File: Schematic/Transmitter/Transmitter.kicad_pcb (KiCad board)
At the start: 2 copper layers, 141.8 x 96.5 mm, 4 parts, among them J2 Remote Umbilical, U1 Mini360, U2 RFM69HW, U3 BP

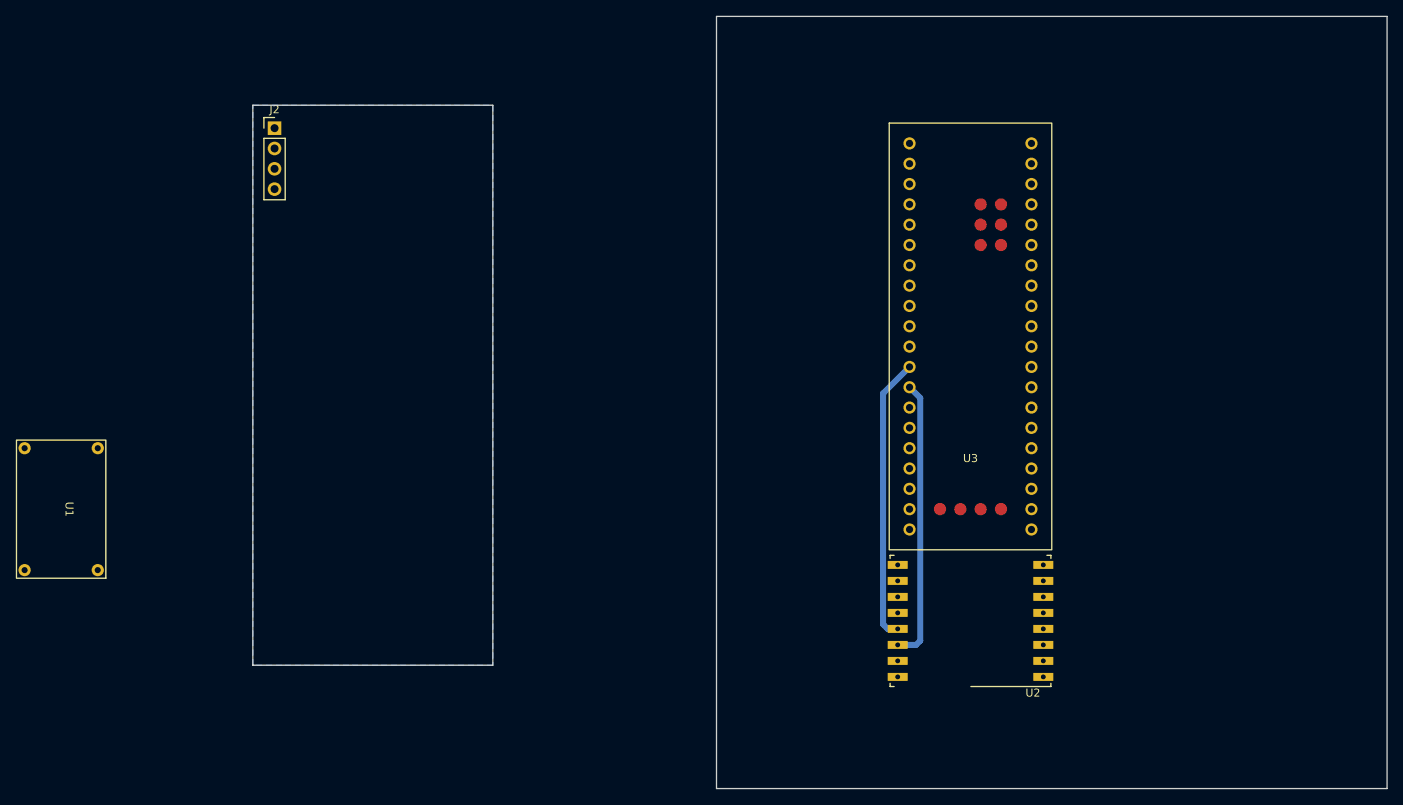
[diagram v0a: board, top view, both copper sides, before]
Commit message: Add transmitter PCB
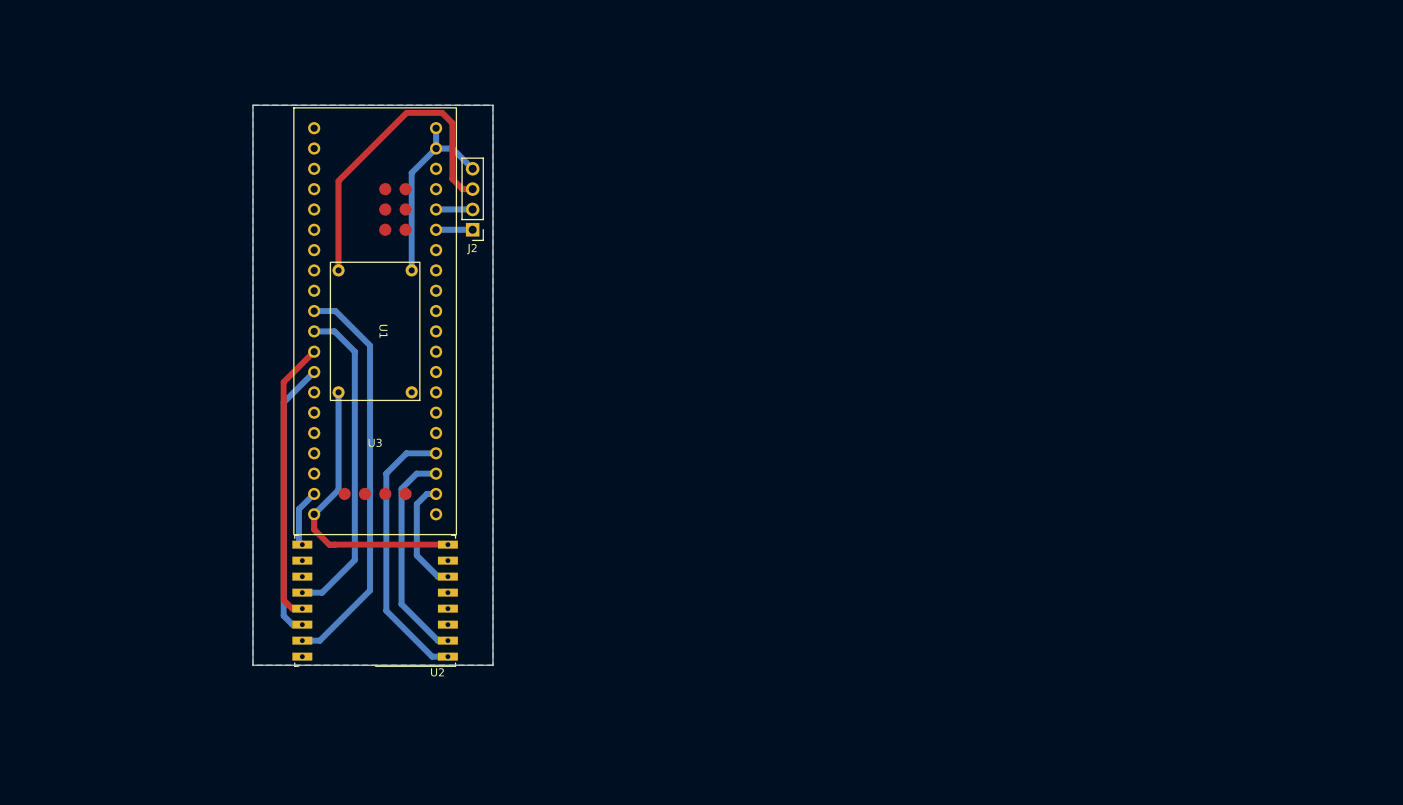
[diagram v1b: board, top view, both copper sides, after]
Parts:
- moved U2 74.5 mm to (145.3, 121.9)
- moved U3 74.4 mm to (145.3, 85.7)
- moved U1 45.1 mm to (145.3, 88.3)
- moved J2 27.8 mm to (157.5, 75.6), turned to 180 degrees
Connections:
- U3 pad PA0: /PPM IN -> unconnected-(U3-PadPA0)
- U3 pad PA1: /PPM OUT -> unconnected-(U3-PadPA1)
- U3 pad PA4: /NSS -> unconnected-(U3-PadPA4)
- U3 pad PA5: /SCK -> unconnected-(U3-PadPA5)
- U3 pad PA6: /MISO -> unconnected-(U3-PadPA6)
- U3 pad PA7: /MOSI -> unconnected-(U3-PadPA7)
- U3 pad PB10: unconnected-(U3-PadPB10) -> /PPM OUT
- U3 pad PB11: unconnected-(U3-PadPB11) -> /PPM IN
- U3 pad PB12: /NSS -> unconnected-(U3-PadPB12)
- U3 pad PB13: /SCK -> unconnected-(U3-PadPB13)
- U3 pad PB14: /MISO -> unconnected-(U3-PadPB14)
- U3 pad PB15: /MOSI -> unconnected-(U3-PadPB15)
- U3 pad PB6: /AUX -> unconnected-(U3-PadPB6)
- U3 pad PB7: /INTER -> unconnected-(U3-PadPB7)
- U3 pad PB8: /RESET -> unconnected-(U3-PadPB8)
- U3 pad PC13: unconnected-(U3-PadPC13) -> /AUX
- U3 pad PC14: unconnected-(U3-PadPC14) -> /INTER
- U3 pad PC15: unconnected-(U3-PadPC15) -> /RESET
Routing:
- net /NSS: track 0.00 -> 50.4 mm
- net /SCK: track 0.00 -> 40.4 mm
- net +BATT: track 0.00 -> 39.5 mm
- net +3V3: track 0.00 -> 35.9 mm
- net /RESET: track 0.00 -> 34.5 mm
- net GND: track 0.00 -> 32.0 mm
- net /INTER: track 0.00 -> 27.2 mm
- net /AUX: track 0.00 -> 14.4 mm
- net /PPM IN: track 0.00 -> 4.57 mm
- net /PPM OUT: track 0.00 -> 4.57 mm
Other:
- board size 141.8 x 96.5 mm -> 30 x 70 mm

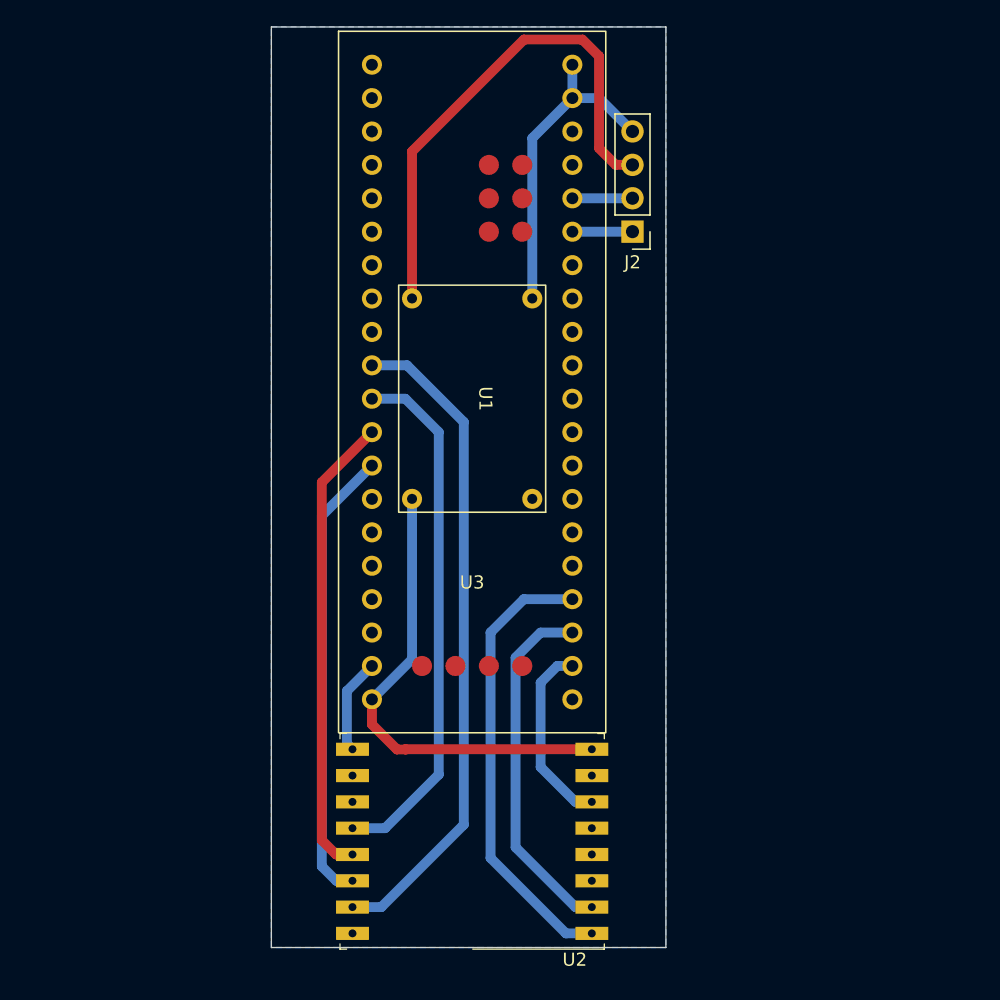
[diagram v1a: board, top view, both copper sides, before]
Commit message: combine schematics into a single PCB layout
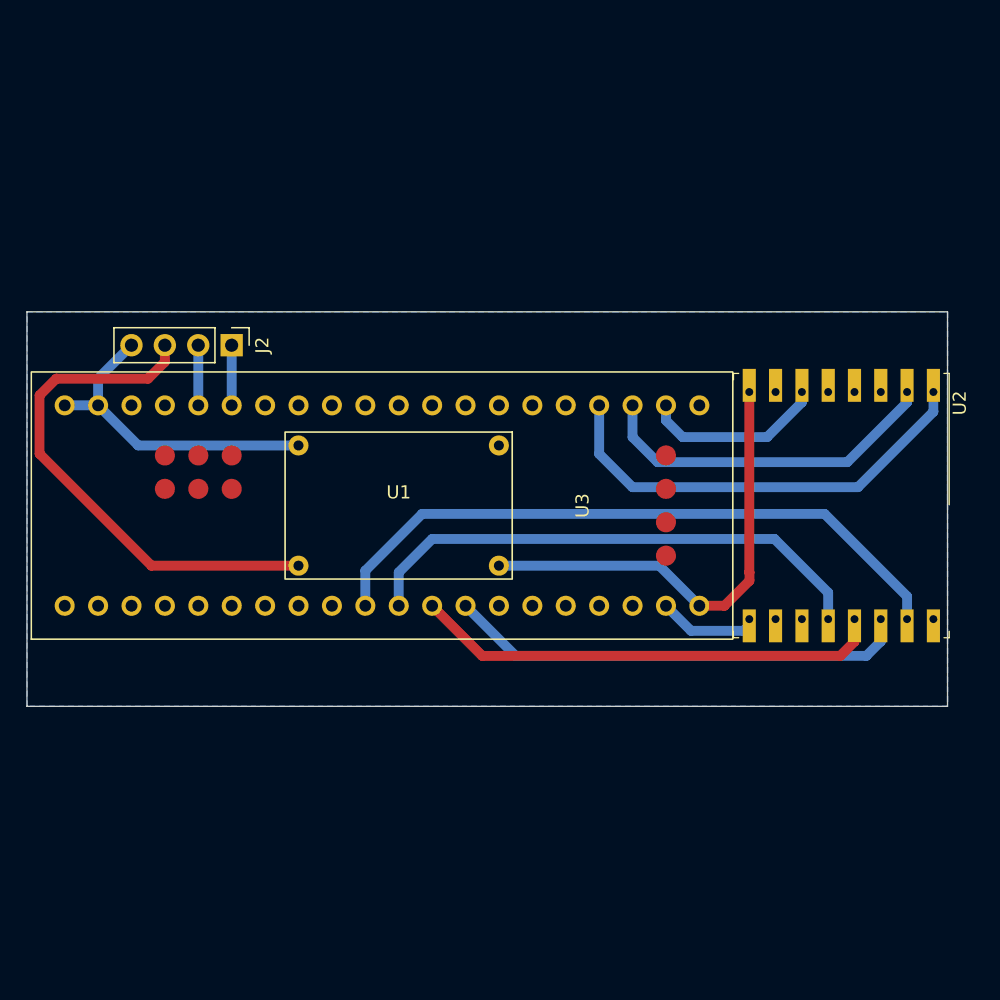
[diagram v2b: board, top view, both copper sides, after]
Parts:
- moved U2 37.9 mm to (173.4, 96.4), turned to -90 degrees
- moved J2 31.7 mm to (127.0, 84.2), turned to -90 degrees
- moved U3 13.4 mm to (137.2, 96.4), turned to 90 degrees
- moved U1 9.86 mm to (139.7, 96.4), turned to 0 degrees
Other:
- board size 30 x 70 mm -> 70 x 30 mm

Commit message: Work on transmitter breakout
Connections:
- U3 pad PA15: /NSS -> unconnected-(U3-PadPA15)
- U3 pad PA4: unconnected-(U3-PadPA4) -> /NSS
- U3 pad PA5: unconnected-(U3-PadPA5) -> /SCK
- U3 pad PA6: unconnected-(U3-PadPA6) -> /MISO
- U3 pad PA7: unconnected-(U3-PadPA7) -> /MOSI
- U3 pad PB3: /SCK -> unconnected-(U3-PadPB3)
- U3 pad PB4: /MISO -> unconnected-(U3-PadPB4)
- U3 pad PB5: /MOSI -> unconnected-(U3-PadPB5)
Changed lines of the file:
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@@
   (net 34 "unconnected-(U3-PadSWO)")
   (net 35 "unconnected-(U3-Vbat-PadVBAT)")
-  (net 36 "unconnected-(U3-PadPA4)")
-  (net 37 "unconnected-(U3-PadPA5)")
-  (net 38 "unconnected-(U3-PadPA6)")
-  (net 39 "unconnected-(U3-PadPA7)")
+  (net 36 "unconnected-(U3-PadPA15)")
+  (net 37 "unconnected-(U3-PadPB3)")
+  (net 38 "unconnected-(U3-PadPB4)")
+  (net 39 "unconnected-(U3-PadPB5)")
   (net 40 "unconnected-(U3-PadPB12)")
   (net 41 "unconnected-(U3-PadPB13)")
@@
       (net 23 "unconnected-(U3-PadPA3)") (pinfunction "PA3") (pintype "bidirectional+no_connect"))
     (pad "PA4" thru_hole circle (at 7.62 5.08 90) (size 1.524 1.524) (drill 0.9) (layers "*.Cu" "*.Mask")
-      (net 36 "unconnected-(U3-PadPA4)") (pinfunction "PA4") (pintype "bidirectional+no_connect"))
+      (net 17 "/NSS") (pinfunction "PA4") (pintype "bidirectional"))
     (pad "PA5" thru_hole circle (at 7.62 2.54 90) (size 1.524 1.524) (drill 0.9) (layers "*.Cu" "*.Mask")
-      (net 37 "unconnected-(U3-PadPA5)") (pinfunction "PA5") (pintype "bidirectional+no_connect"))
+      (net 14 "/SCK") (pinfunction "PA5") (pintype "bidirectional"))
     (pad "PA6" thru_hole circle (at 7.62 0 90) (size 1.524 1.524) (drill 0.9) (layers "*.Cu" "*.Mask")
-      (net 38 "unconnected-(U3-PadPA6)") (pinfunction "PA6") (pintype "bidirectional+no_connect"))
+      (net 15 "/MISO") (pinfunction "PA6") (pintype "bidirectional"))
     (pad "PA7" thru_hole circle (at 7.62 -2.54 90) (size 1.524 1.524) (drill 0.9) (layers "*.Cu" "*.Mask")
-      (net 39 "unconnected-(U3-PadPA7)") (pinfunction "PA7") (pintype "bidirectional+no_connect"))
+      (net 16 "/MOSI") (pinfunction "PA7") (pintype "bidirectional"))
     (pad "PA8" thru_hole circle (at -7.62 -12.7 90) (size 1.524 1.524) (drill 0.9) (layers "*.Cu" "*.Mask")
       (net 24 "unconnected-(U3-PadPA8)") (pinfunction "PA8") (pintype "bidirectional+no_connect"))
@@
       (net 28 "unconnected-(U3-PadPA12)") (pinfunction "PA12") (pintype "bidirectional+no_connect"))
     (pad "PA15" thru_hole circle (at -7.62 0 90) (size 1.524 1.524) (drill 0.9) (layers "*.Cu" "*.Mask")
-      (net 17 "/NSS") (pinfunction "PA15") (pintype "bidirectional"))
+      (net 36 "unconnected-(U3-PadPA15)") (pinfunction "PA15") (pintype "bidirectional"))
     (pad "PB0" thru_hole circle (at 7.62 -5.08 90) (size 1.524 1.524) (drill 0.9) (layers "*.Cu" "*.Mask")
       (net 29 "unconnected-(U3-PadPB0)") (pinfunction "PB0") (pintype "bidirectional+no_connect"))
@@
       (net 31 "unconnected-(U3-BOOT1-PadPB2)") (pinfunction "BOOT1") (pintype "bidirectional+no_connect"))
     (pad "PB3" thru_hole circle (at -7.62 2.54 90) (size 1.524 1.524) (drill 0.9) (layers "*.Cu" "*.Mask")
-      (net 14 "/SCK") (pinfunction "PB3") (pintype "bidirectional"))
+      (net 37 "unconnected-(U3-PadPB3)") (pinfunction "PB3") (pintype "bidirectional"))
     (pad "PB4" thru_hole circle (at -7.62 5.08 90) (size 1.524 1.524) (drill 0.9) (layers "*.Cu" "*.Mask")
-      (net 15 "/MISO") (pinfunction "PB4") (pintype "bidirectional"))
+      (net 38 "unconnected-(U3-PadPB4)") (pinfunction "PB4") (pintype "bidirectional"))
     (pad "PB5" thru_hole circle (at -7.62 7.62 90) (size 1.524 1.524) (drill 0.9) (layers "*.Cu" "*.Mask")
-      (net 16 "/MOSI") (pinfunction "PB5") (pintype "bidirectional"))
+      (net 39 "unconnected-(U3-PadPB5)") (pinfunction "PB5") (pintype "bidirectional"))
     (pad "PB6" thru_hole circle (at -7.62 10.16 90) (size 1.524 1.524) (drill 0.9) (layers "*.Cu" "*.Mask")
       (net 46 "unconnected-(U3-PadPB6)") (pinfunction "PB6") (pintype "bidirectional+no_connect"))
@@
       (net 5 "+3V3") (pinfunction "OUT") (pintype "power_out"))
   )
-  (gr_rect (start 111.435 111.661) (end 181.435 81.661)
+  (gr_rect (start 111.435 81.661) (end 181.435 111.661)
     (stroke (width 0.1) (type default)) (fill none) (layer "Edge.Cuts"))
   (segment (start 127 84.201) (end 127 88.768) (width 0.75) (layer "B.Cu") (net 1))
